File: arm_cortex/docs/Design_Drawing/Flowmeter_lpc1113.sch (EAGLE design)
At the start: 79 parts, among them IC2 OP07CN, IC5 OP07CN, U1 LPC1113FBD48/302,1, U2 LD1117S33CTR, U4 MAX232ACSE+, U5 MAX485CSA+, U6 7805TV, U7 MCP4921-E/P, U8 SP1490, X1 MKDSN1,5/3-5,08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

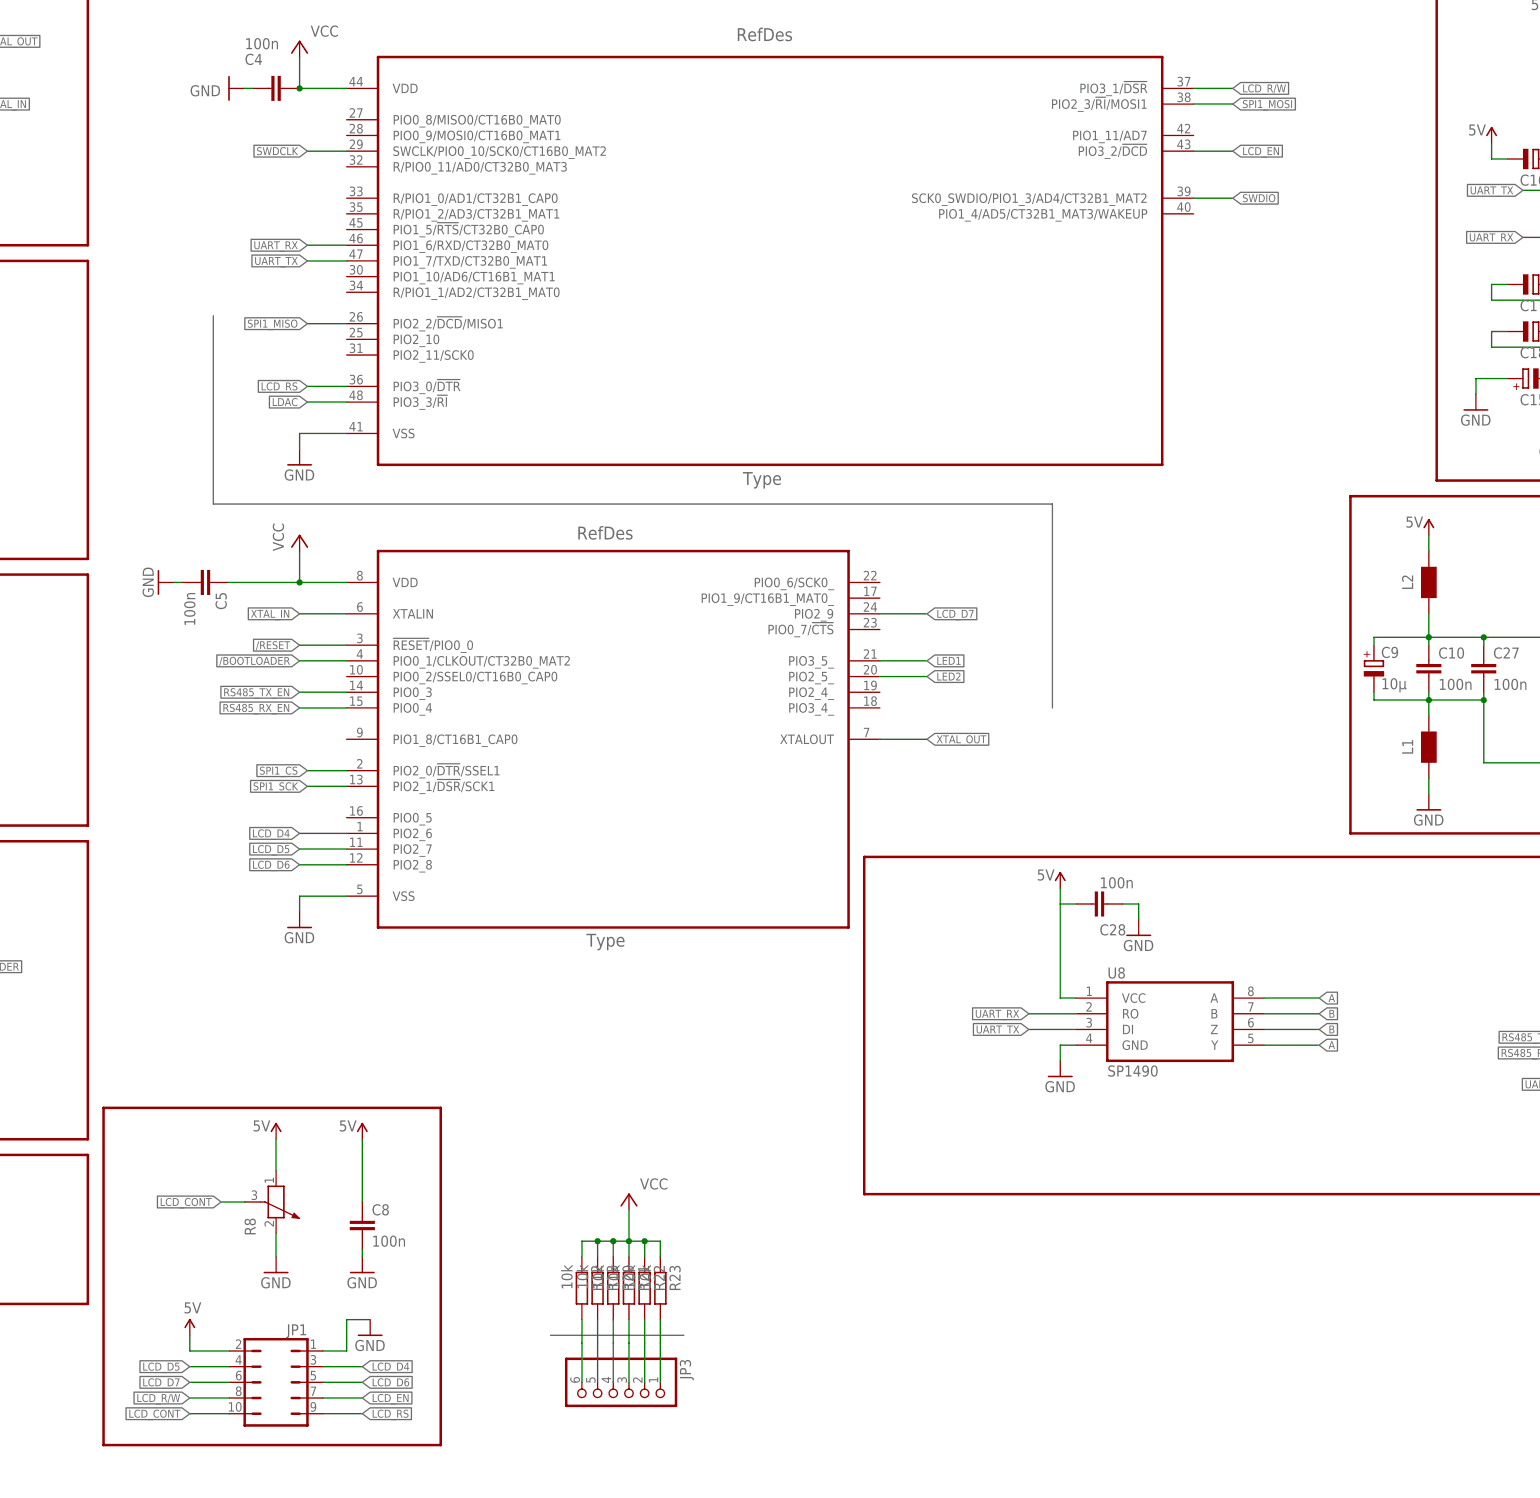
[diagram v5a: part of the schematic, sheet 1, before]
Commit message: 
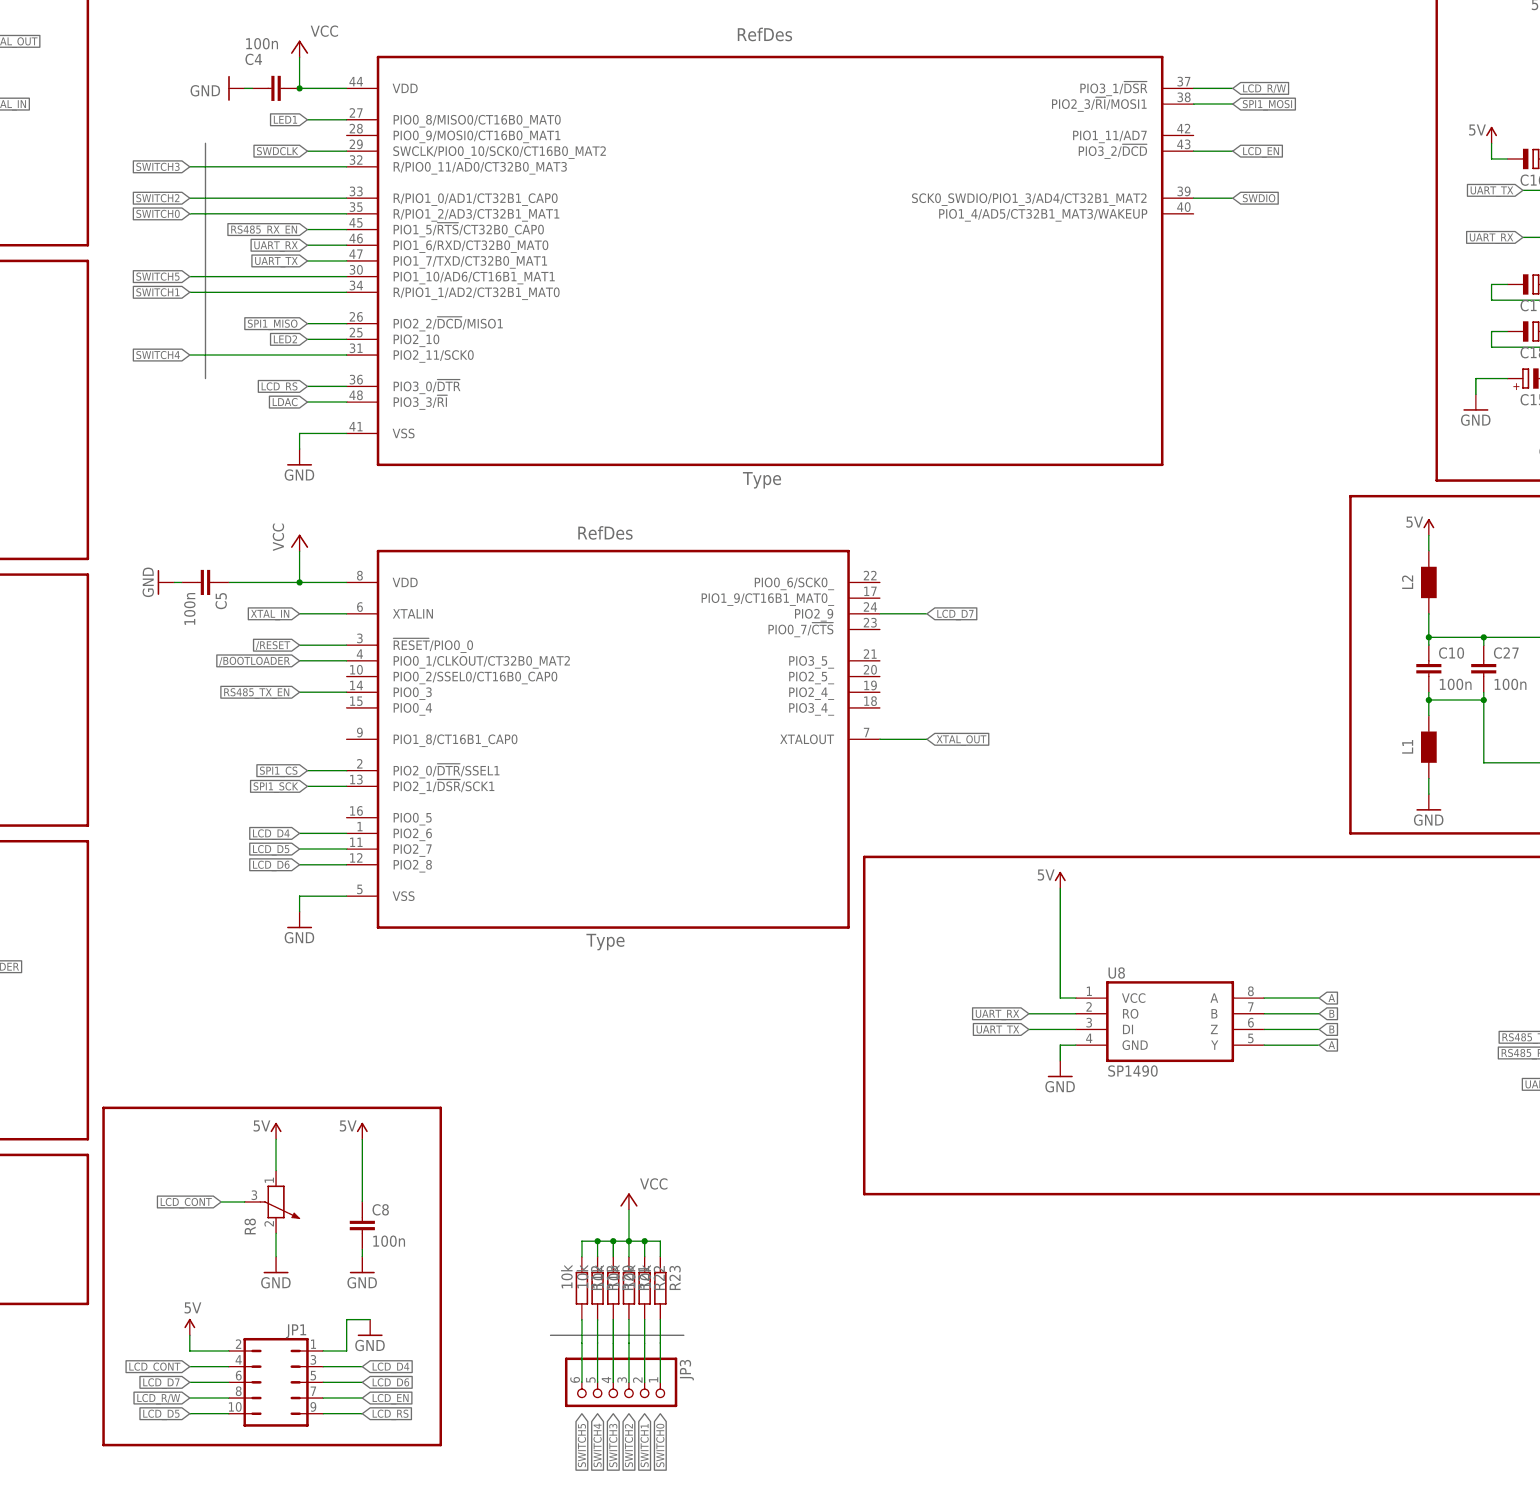
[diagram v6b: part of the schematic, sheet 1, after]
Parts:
- removed C28: 100n, rcl:C-EUC0805K
- removed C9: 10µ, rcl:CPOL-EUCT3528
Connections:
- removed net N$43: C11.2, C13.+, U2.VOUT, U2.VOUT_2
- net +12V: now also R15.1
- net 5V: no longer C28.2
- net GND: no longer C28.1
- net GND1: no longer C9.-
- net LCD_CONT: now also JP1.4; no longer JP1.10
- net LCD_D5: now also JP1.10; no longer JP1.4
- net LED1: now also U1B.PIO0_8/MISO0/CT16B0_MAT0; no longer U1A.PIO3_5_
- net LED2: now also U1B.PIO2_10; no longer U1A.PIO2_5_
- net N$11: no longer C9.+
- net N$27: no longer R15.1
- net RS485_RX_EN: now also U1B.PIO1_5/!RTS!/CT32B0_CAP0; no longer U1A.PIO0_4
- net SWITCH0: now also U1B.R/PIO1_2/AD3/CT32B1_MAT1
- net SWITCH1: now also U1B.R/PIO1_1/AD2/CT32B1_MAT0
- net SWITCH2: now also U1B.R/PIO1_0/AD1/CT32B1_CAP0
- net SWITCH3: now also U1B.R/PIO0_11/AD0/CT32B0_MAT3
- net SWITCH4: now also U1B.PIO2_11/SCK0
- net SWITCH5: now also U1B.PIO1_10/AD6/CT16B1_MAT1
- net VCC: now also C11.2, C13.+, U2.VOUT, U2.VOUT_2

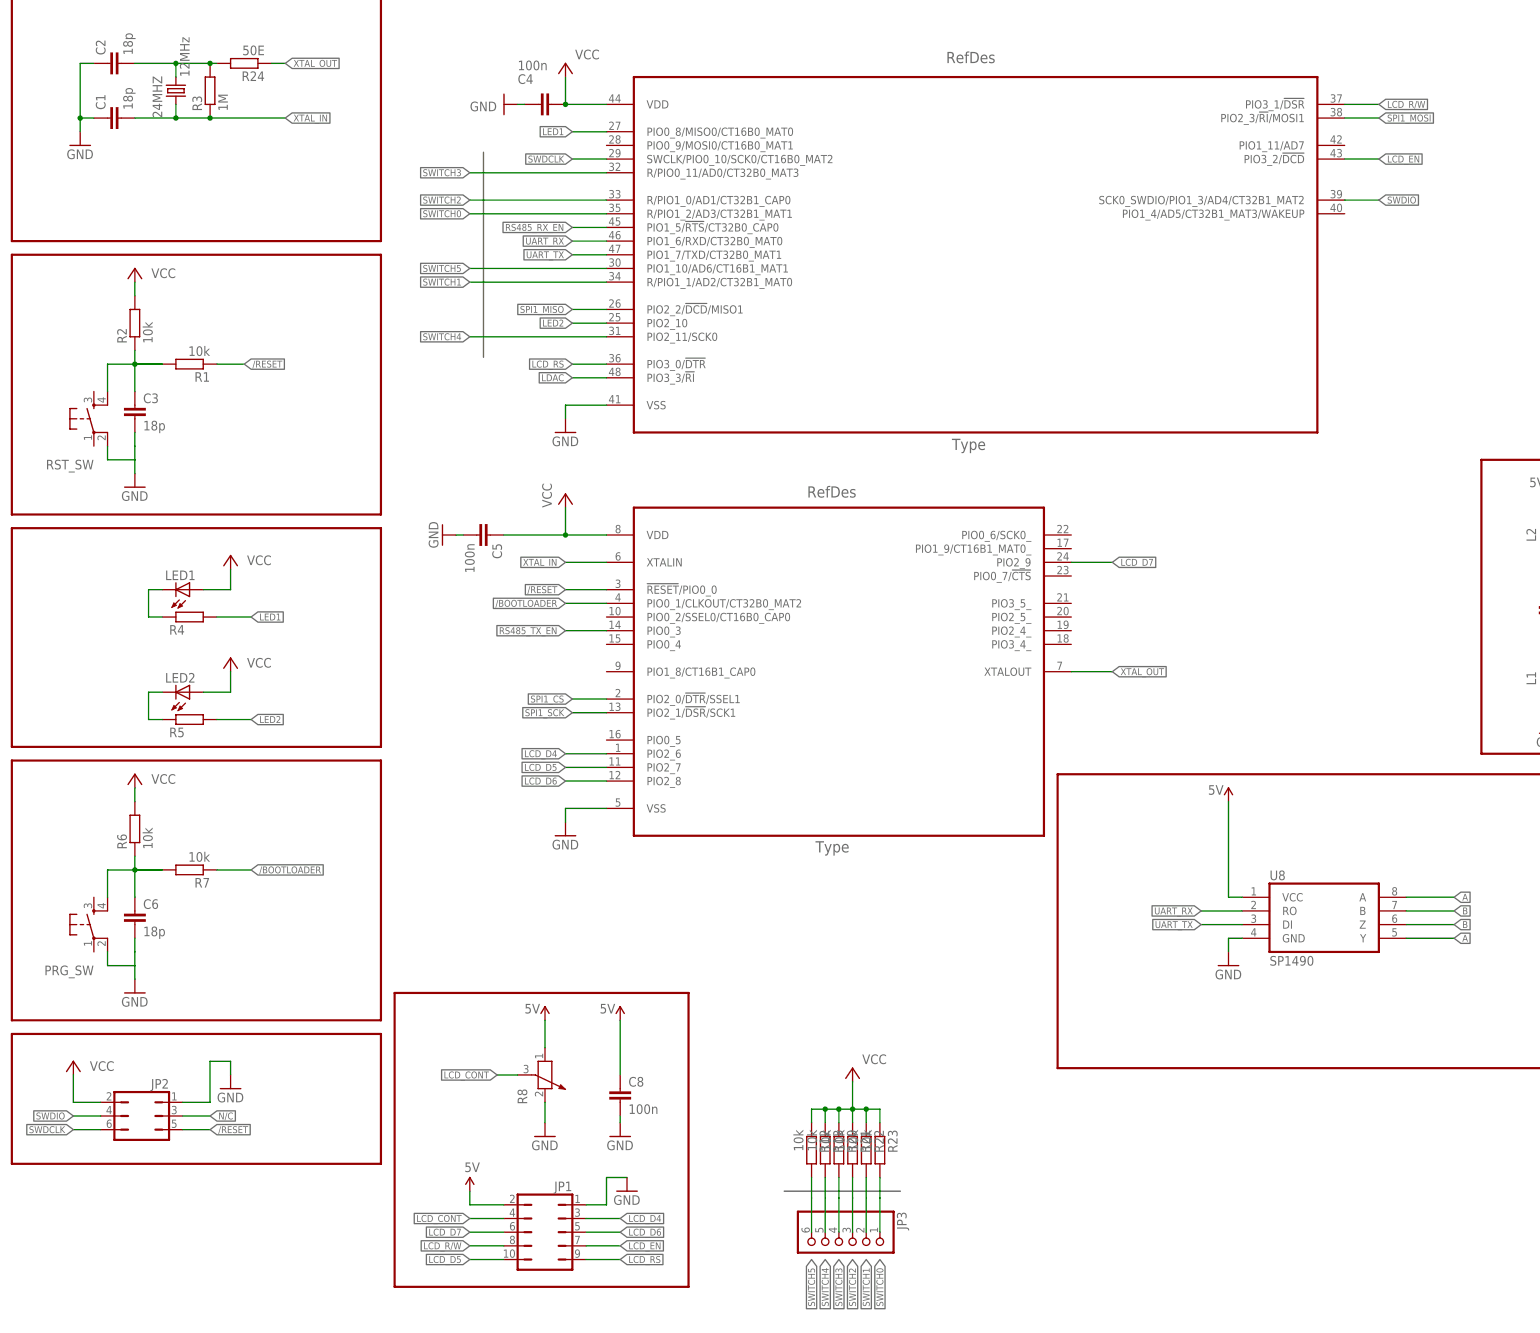
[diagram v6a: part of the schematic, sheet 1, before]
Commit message: single layer board
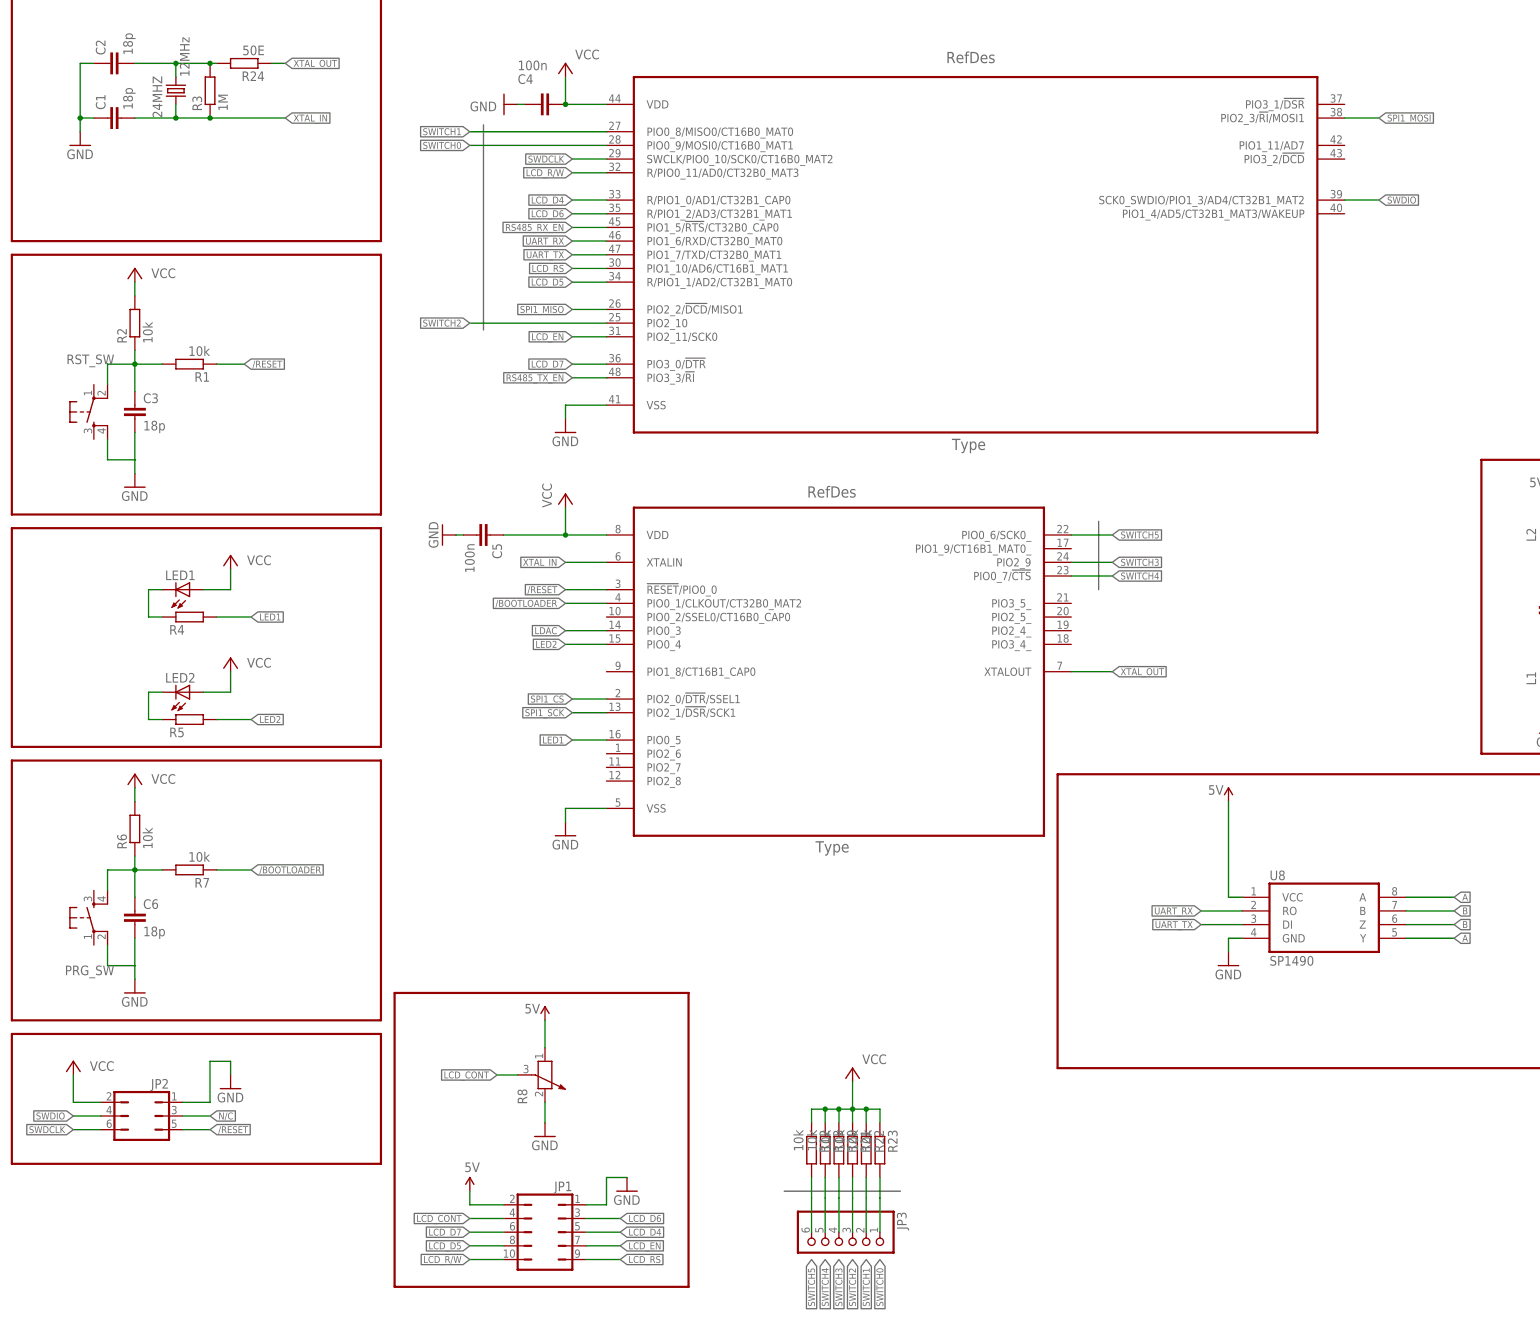
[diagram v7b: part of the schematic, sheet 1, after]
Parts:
- removed C22: 100n, rcl:C-EU025-024X044
- removed C8: 100n, rcl:C-EUC0805K
- added R25: 10k, rcl:R-EU_R0805W
- added R26: 22k, rcl:R-EU_R0805W
- C23: value 100uF/60V -> 100n; device rcl:CPOL-EUE5-6 -> rcl:C-EUC0805K
- PRG_SW, RST_SW: device SparkFun1:TAC_SWITCHSMD -> SparkFun1:TAC_SWITCHPTH
- R14, R15, R16, R17, R18: device rcl:R-EU_0207/10 -> rcl:R-EU_R0805W
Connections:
- removed net N$22: C23.+, C25.1, IC2.V+
- new net N$7: IC2.+IN, R25.2, R26.1
- net +12V: now also C25.1, IC2.V+
- net 5V: no longer C8.1
- net GND: now also C23.2, RST_SW.4; no longer C22.2, C23.-, C8.2, RST_SW.2
- net LCD_D4: now also JP1.5, U1B.R/PIO1_0/AD1/CT32B1_CAP0; no longer JP1.3, U1A.PIO2_6
- net LCD_D5: now also JP1.8, U1B.R/PIO1_1/AD2/CT32B1_MAT0; no longer JP1.10, U1A.PIO2_7
- net LCD_D6: now also JP1.3, U1B.R/PIO1_2/AD3/CT32B1_MAT1; no longer JP1.5, U1A.PIO2_8
- net LCD_D7: now also U1B.PIO3_0/!DTR!; no longer U1A.PIO2_9
- net LCD_EN: now also U1B.PIO2_11/SCK0; no longer U1B.PIO3_2/!DCD!
- net LCD_R/W: now also JP1.10, U1B.R/PIO0_11/AD0/CT32B0_MAT3; no longer JP1.8, U1B.PIO3_1/!DSR!
- net LCD_RS: now also U1B.PIO1_10/AD6/CT16B1_MAT1; no longer U1B.PIO3_0/!DTR!
- net LDAC: now also U1A.PIO0_3; no longer U1B.PIO3_3/!RI!
- net LED1: now also U1A.PIO0_5; no longer U1B.PIO0_8/MISO0/CT16B0_MAT0
- net LED2: now also U1A.PIO0_4; no longer U1B.PIO2_10
- net N$15: now also C23.1; no longer C22.1
- net N$37: now also R26.2
- net N$4: now also RST_SW.2; no longer RST_SW.4
- net RS485_TX_EN: now also U1B.PIO3_3/!RI!; no longer U1A.PIO0_3
- net SENSOR_SIGNAL: now also R25.1; no longer IC2.+IN
- net SWITCH0: now also U1B.PIO0_9/MOSI0/CT16B0_MAT1; no longer U1B.R/PIO1_2/AD3/CT32B1_MAT1
- net SWITCH1: now also U1B.PIO0_8/MISO0/CT16B0_MAT0; no longer U1B.R/PIO1_1/AD2/CT32B1_MAT0
- net SWITCH2: now also U1B.PIO2_10; no longer U1B.R/PIO1_0/AD1/CT32B1_CAP0
- net SWITCH3: now also U1A.PIO2_9; no longer U1B.R/PIO0_11/AD0/CT32B0_MAT3
- net SWITCH4: now also U1A.PIO0_7/!CTS!; no longer U1B.PIO2_11/SCK0
- net SWITCH5: now also U1A.PIO0_6/SCK0_; no longer U1B.PIO1_10/AD6/CT16B1_MAT1
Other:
- moved on the sheet: PRG_SW, RST_SW
